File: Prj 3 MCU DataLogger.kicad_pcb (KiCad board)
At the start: 2 copper layers, 55.9 x 35.5 mm, 30 parts, among them J1 Conn_01x04_Male, J2 Conn_01x04_Male, J3 Conn_01x09_Male, J4 Conn_02x03_Odd_Even, U1 24LC1025, U2 24LC1025, U3 DS1337S_, U4 ATMEGA328P-AU, Y1 16 MHz, Y2 32.768 KHz

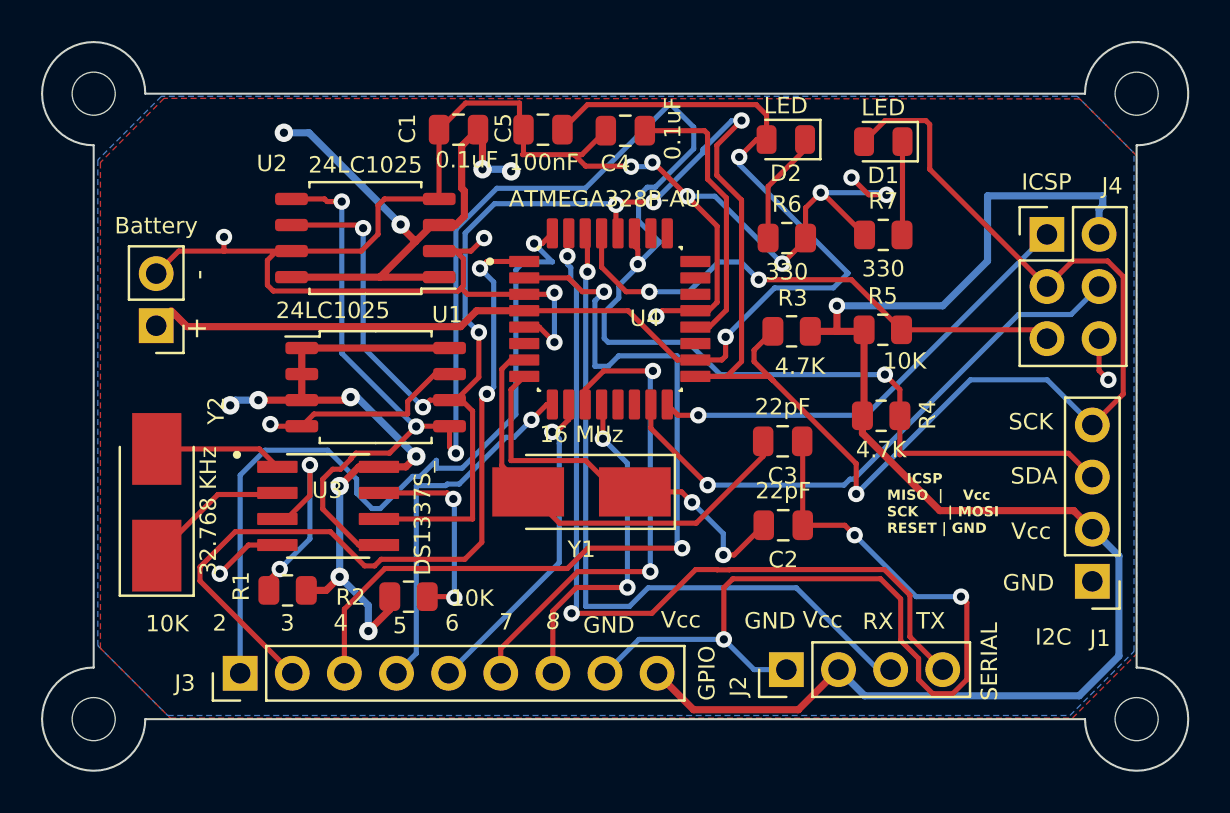
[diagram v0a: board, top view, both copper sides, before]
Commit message: Fixed two defects in the schematic.
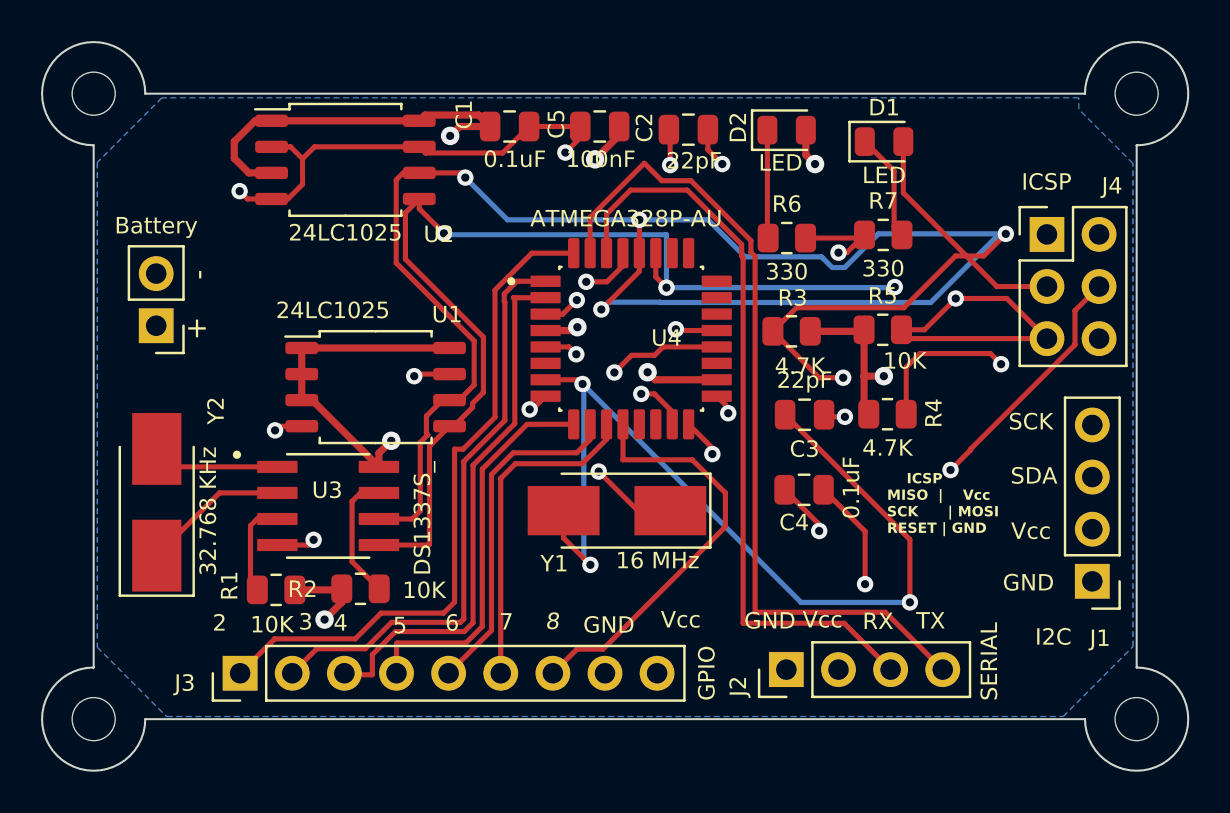
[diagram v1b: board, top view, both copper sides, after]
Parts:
- moved C2 19.8 mm to (116.8, 73.2)
- moved C4 19.5 mm to (122.4, 90.7)
- moved U2 3.93 mm to (100.1, 74.7), turned to 0 degrees
- moved C5 2.77 mm to (112.5, 73.0)
- moved C1 2.49 mm to (108.1, 73.0), turned to 0 degrees
- moved R2 2.37 mm to (100.8, 95.6)
- moved Y1 1.95 mm to (113.3, 91.7)
- moved C3 1.68 mm to (122.5, 87.1)
- moved U4 1.42 mm to (114.0, 83.4)
- moved R1 0.56 mm to (96.7, 95.6)
- moved D2 0.46 mm to (121.6, 73.2), turned to 0 degrees
- moved R4 0.32 mm to (126.5, 87.0)
- turned D1 to 0 degrees
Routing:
- net /Vcc: track 198.1 -> 55.7 mm, vias 14 -> 8
- net GND: track 156.7 -> 43.3 mm, vias 18 -> 12
- net /SDA: track 97.4 -> 72.5 mm, vias 5 -> 4
- net Net-(U4-PB6): track 22.0 -> 46.1 mm, vias 0 -> 3
- net Net-(U4-AREF): track 13.9 -> 30.4 mm, vias 0 -> 2
- net /D4: track 42.5 -> 26.2 mm, vias 2 -> 0
- net /SCK: track 123.2 -> 136.2 mm, vias 7 -> 6
- net /RESET: track 26.0 -> 38.6 mm
- net /D3: track 38.8 -> 28.4 mm, vias 2 -> 0
- net /D7: track 24.3 -> 16.2 mm, vias 2 -> 0
- net Net-(U4-PB7): track 19.8 -> 26.4 mm, vias 2 -> 3
- net /D2: track 39.0 -> 32.7 mm, vias 1 -> 0
- net Net-(U3-~{INTA}): track 10.5 -> 4.71 mm, vias 2 -> 0
- net /D8: track 16.6 -> 20.4 mm, vias 2 -> 0
- net Net-(U3-SQW/~INT): track 9.92 -> 6.29 mm, vias 2 -> 0
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- added copper zone on In2.Cu, net /Vcc
- removed copper zone on F.Cu, net /Vcc
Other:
- copper layers 2 -> 4

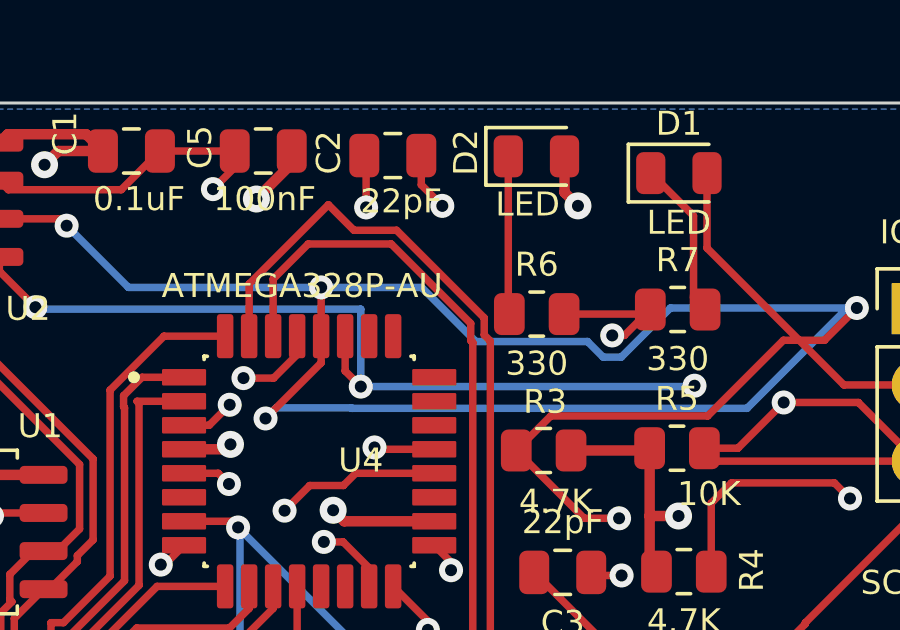
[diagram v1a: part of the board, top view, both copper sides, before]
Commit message: 4layer PCB is fixed from bugs of the schematics.
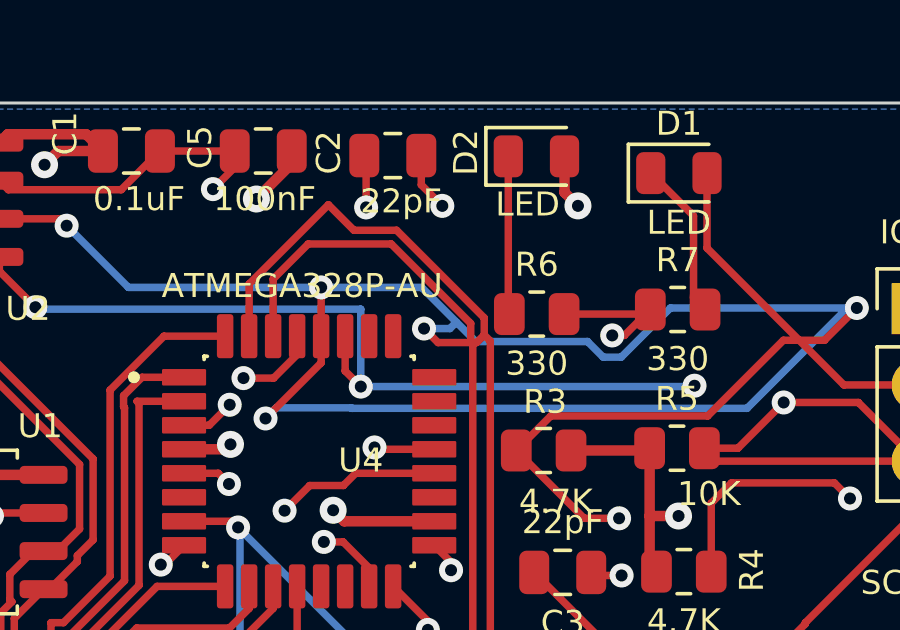
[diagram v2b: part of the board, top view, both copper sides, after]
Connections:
- D1 pad 2: /SCK -> /RX
- J1 pad 4: /SCK -> /RX
- J2 pad 4: /TX -> /RX
- J4 pad 3: /SCK -> /RX
- R3 pad 2: /SCK -> /RX
- U1 pad 6: /SCK -> /RX
- U2 pad 6: /SCK -> /RX
- U3 pad 6: /SCK -> /RX
- U4 pad 17: /SCK -> /RX
- U4 pad 28: /SCK -> /RX
- U4 pad 31: /TX -> /RX
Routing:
- net /RX: track 36.7 -> 217.1 mm, vias 0 -> 7
- net /SCK: track 136.2 -> 0.00 mm, vias 6 -> 0
- net /TX: track 40.7 -> 0.00 mm
